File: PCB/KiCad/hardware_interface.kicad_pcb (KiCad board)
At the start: 6 copper layers, 86 x 86 mm, 252 parts, among them J1 Reset Header, J10 I2C1, J11 I2C1, J12 TIM1, J13 TIM2, J14 I2C2, J15 I2C2, J16 I2C2, J17 I2C2, J18 3.3V Out, J19 5V Out, J2 SWD Flash, J20 UART1, J21 UART2, J22 UART3, J23 Servo 1, J24 Servo 2, J25 GPIO, J26 Analog 1, J27 Analog 2, J28 USB1, J29 USB2, J3 XT30, J30 LED1, J31 LED2, J4 CAN1, J5 CAN1, J6 SPI1, J7 SPI1, J8 I2C1, J9 I2C1, SW1 Reset, SW2 User Button, U1 STM32F429ZIT6TR, U10 USBLC6-2SC6, U11 TCAN1057AVDRQ1, U12 USBLC6-2SC6, U2 TPS2117DRLR, U3 MIC2039AYM6-TR, U4 OPA2834IDGKR, U5 OPA2834IDGKR, U6 SN74S1051DR, U7 SN74S1051DR, U8 SN74S1051DR, U9 SN74S1051DR, Y1 IQXO-791 8.00MHz

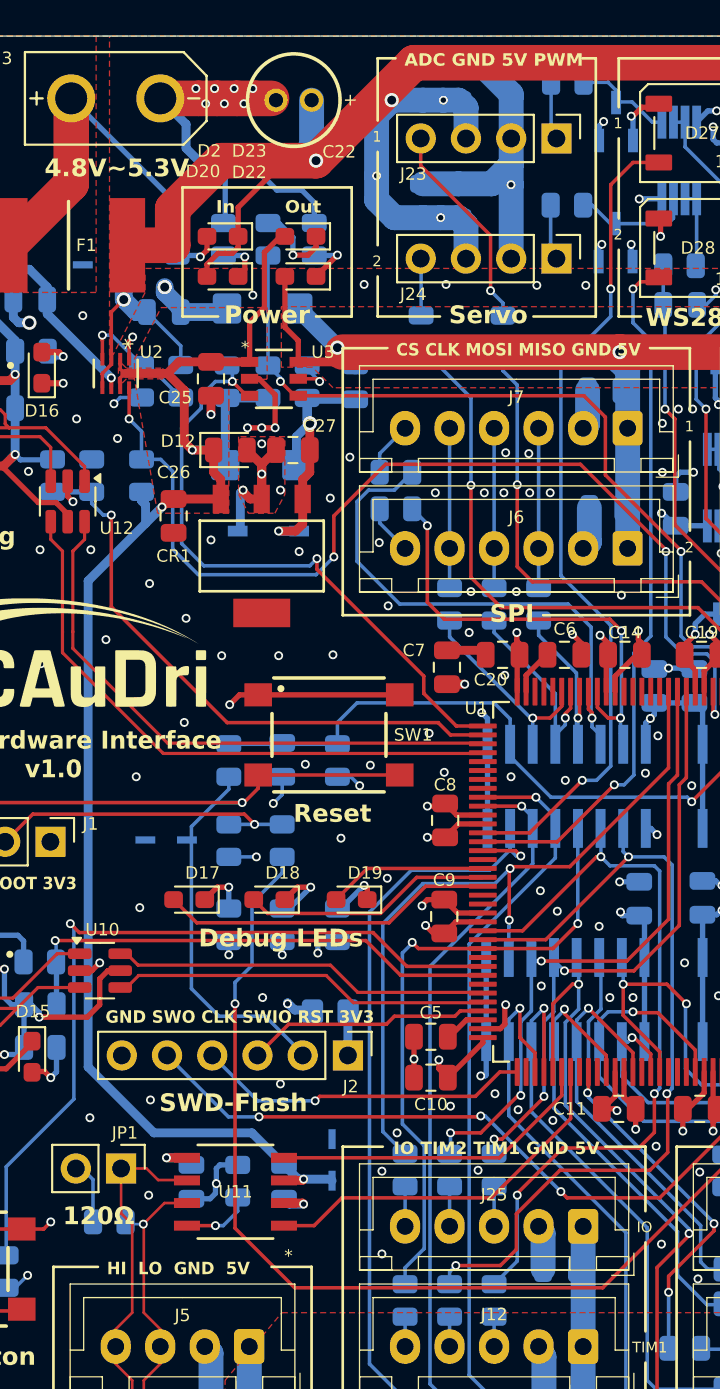
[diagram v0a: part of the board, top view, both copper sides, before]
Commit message: PCB: fix silkscreen pinout for servo and CAN connectors
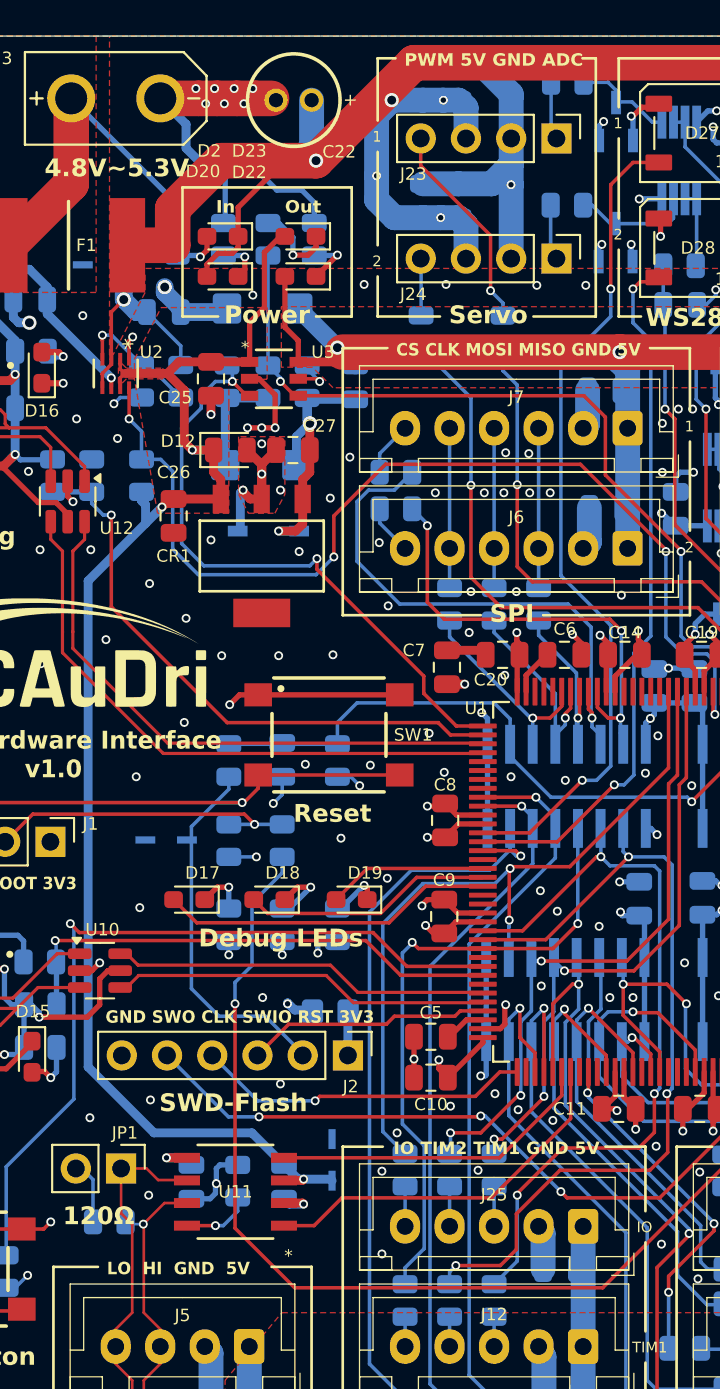
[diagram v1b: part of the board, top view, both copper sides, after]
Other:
- board text added: "LO HI GND 5V"
- board text added: "PWM 5V GND ADC"
- board text removed: "ADC GND 5V PWM"
- board text removed: "HI LO GND 5V"
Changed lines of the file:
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@@
 		)
 	)
-	(gr_text "HI  LO  GND  5V"
+	(gr_text "LO  HI  GND  5V"
 		(at 108.4 124.775 0)
 		(layer "F.SilkS")
@@
 		)
 	)
-	(gr_text "ADC GND 5V PWM"
+	(gr_text "PWM 5V GND ADC"
 		(at 125.11 56.9 0)
 		(layer "F.SilkS")
